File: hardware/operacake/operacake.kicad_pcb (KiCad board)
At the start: 4 copper layers, 120 x 75 mm, 152 parts, among them J1 CONN_02X20, J2 CONN_02X20, P1 ADDRESS, P20 GPIO, P22 I2S, P28 SD, P9 BASEBAND, U1 MASWSS0129, U10 74LVC1G58, U11 74LVC1G58, U12 74LVC1G58, U13 74LVC1G58, U14 74AHC1G02, U15 74AHC1G02, U16 74LVC1G19, U2 SKY13322, U3 SKY13322, U4 PCA9557, U5 TC7MBL3245CFT, U6 74LVC1G58, U7 74LVC1G58, U8 74AHC1G08, U9 74AHC1G08

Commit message: Moved via
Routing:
- net VCC: track 56.9 -> 55.6 mm
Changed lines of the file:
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@@
     (links 598)
     (no_connects 1)
-    (area 59.809499 99.809499 180.190501 175.190501)
+    (area 57.771558 99.809499 182.228443 175.190501)
     (thickness 1.6002)
     (drawings 148)
-    (tracks 1290)
+    (tracks 1287)
     (zones 0)
     (modules 152)
@@
   )
   (setup
-    (last_trace_width 0.2794)
+    (last_trace_width 0.3048)
     (user_trace_width 0.1524)
     (user_trace_width 0.2032)
@@
   (segment (start 131.50596 132.07238) (end 131.04622 132.53212) (width 0.2794) (layer C1F) (net 1))
   (segment (start 142.075 126.4919) (end 142.06728 126.49962) (width 0.2794) (layer C1F) (net 1))
+  (segment (start 132.55752 129.98196) (end 132.55752 129.06756) (width 0.3048) (layer C1F) (net 2) (status 400000))
+  (via (at 132.64896 128.97612) (size 1.0668) (drill 0.635) (layers C1F C4B) (net 2))
+  (segment (start 132.65 128.97508) (end 132.65 127.95) (width 0.3048) (layer C1F) (net 2) (status 800000))
+  (segment (start 128.80086 129.97434) (end 129.92862 129.97434) (width 0.2794) (layer C1F) (net 2) (status 400000))
+  (via (at 129.93116 129.9718) (size 1.0668) (drill 0.635) (layers C1F C4B) (net 2))
   (segment (start 127.87884 116.12118) (end 127.87884 116.49456) (width 0.2794) (layer C1F) (net 2))
   (via (at 128.31318 116.9289) (size 1.0668) (drill 0.635) (layers C1F C4B) (net 2))
@@
   (segment (start 116.336777 128.975619) (end 116.280396 129.032) (width 0.3048) (layer C1F) (net 2))
   (segment (start 116.280396 129.032) (end 114.9604 129.032) (width 0.3048) (layer C1F) (net 2))
-  (segment (start 132.65 127.95) (end 132.55752 128.04248) (width 0.3048) (layer C1F) (net 2) (status 30))
-  (segment (start 132.55752 128.04248) (end 132.55752 129.98196) (width 0.3048) (layer C1F) (net 2) (status 30))
-  (segment (start 132.55752 129.98196) (end 132.55752 129.7686) (width 0.3048) (layer C1F) (net 2) (status 30))
-  (segment (start 132.55752 129.7686) (end 133.28904 129.03708) (width 0.3048) (layer C1F) (net 2) (status 10))
-  (via (at 133.28904 129.03708) (size 1.0668) (drill 0.635) (layers C1F C4B) (net 2))
   (segment (start 128.65 127.95) (end 128.65 129.82348) (width 0.3048) (layer C1F) (net 2) (status 30))
-  (segment (start 128.65 129.82348) (end 128.95172 129.82348) (width 0.3048) (layer C1F) (net 2) (status 30))
-  (segment (start 128.95172 129.82348) (end 129.48666 129.28854) (width 0.3048) (layer C1F) (net 2) (status 10))
-  (via (at 129.48666 129.28854) (size 1.0668) (drill 0.635) (layers C1F C4B) (net 2))
   (segment (start 132.0546 120.61876) (end 132.0546 122.47626) (width 0.3048) (layer C1F) (net 2) (status 30))
   (segment (start 132.0546 122.47626) (end 131.93268 122.59818) (width 0.3048) (layer C1F) (net 2) (status 30))

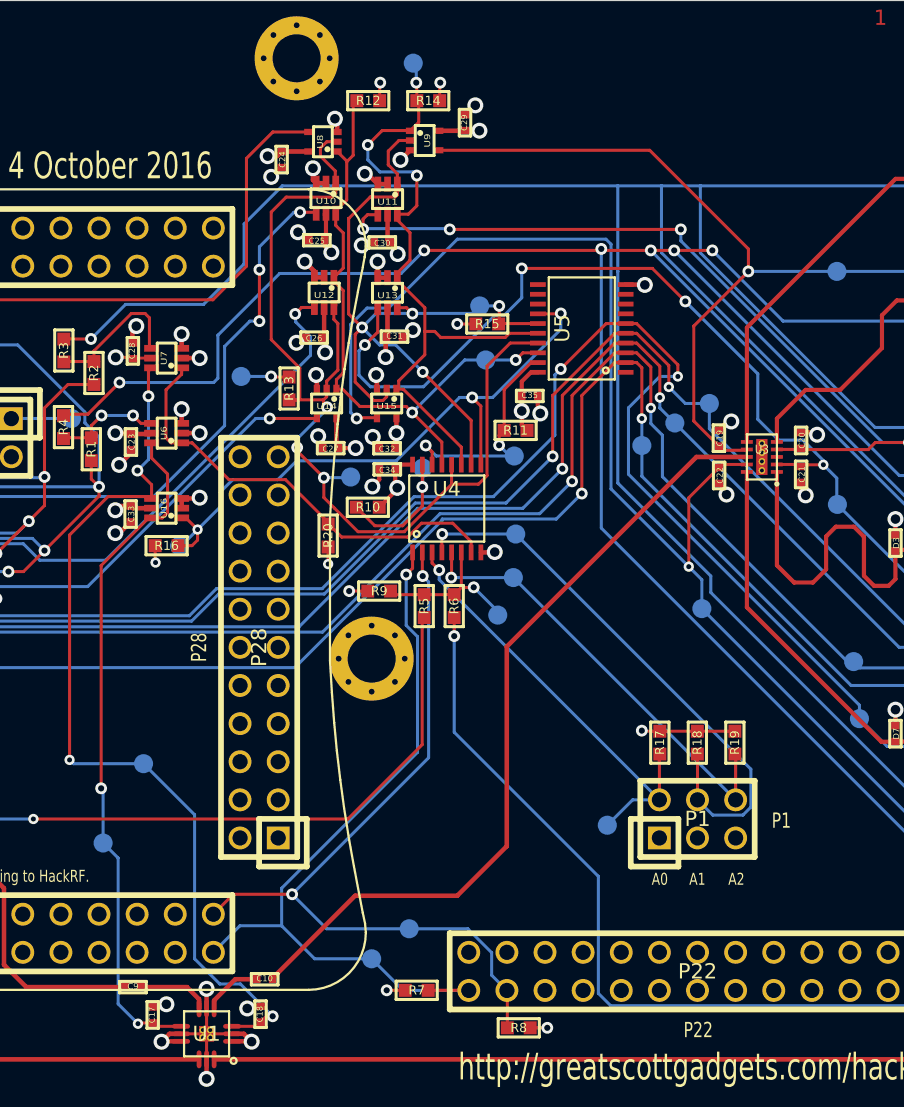
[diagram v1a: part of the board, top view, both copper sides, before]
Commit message: Moved vias.
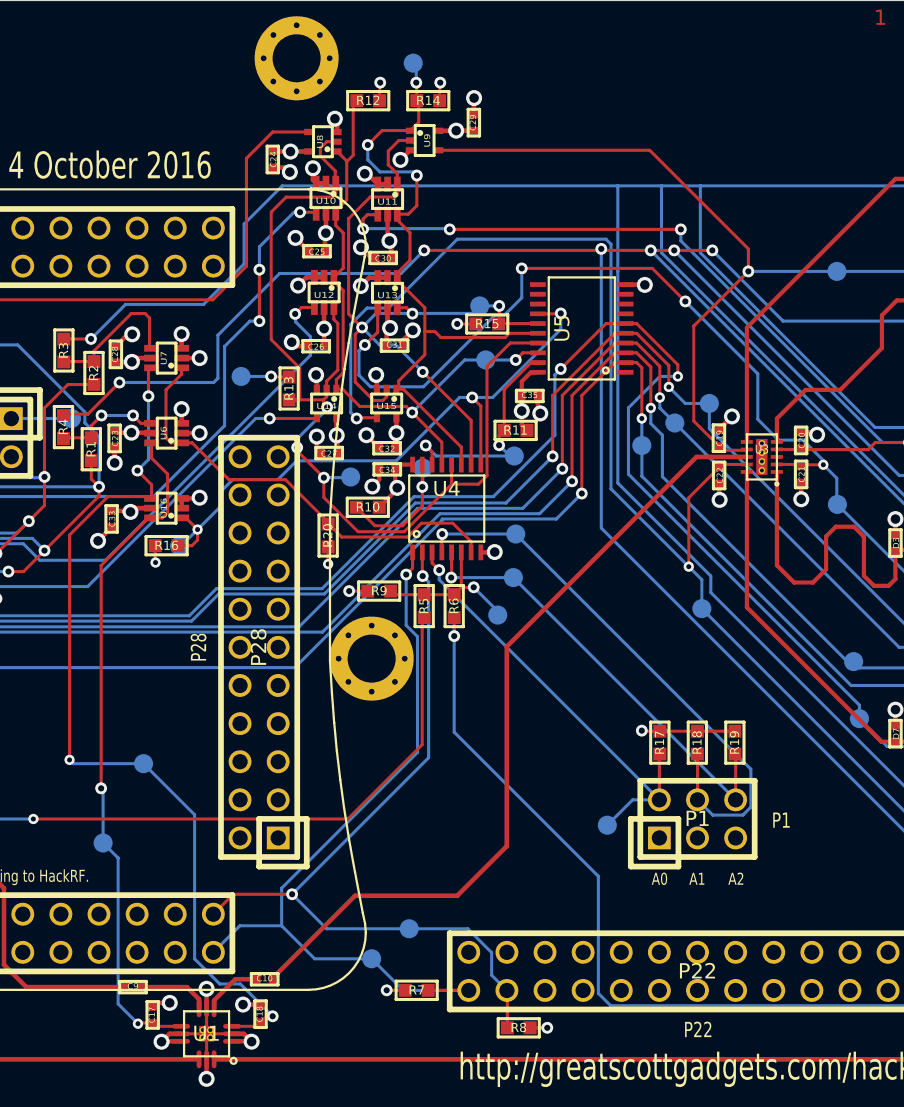
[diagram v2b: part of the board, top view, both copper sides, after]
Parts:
- moved C33 1.30 mm to (113.7, 134.7)
- moved C28 1.15 mm to (114.0, 123.7)
- moved C23 1.11 mm to (113.9, 129.3)
- moved C30 1.04 mm to (131.8, 117.3)
- moved C25 0.73 mm to (127.4, 116.9)
- moved C31 0.60 mm to (132.5, 123.1)
- moved C26 0.59 mm to (127.3, 123.2)
- moved C29 0.59 mm to (137.8, 108.3)
- moved C24 0.59 mm to (124.4, 110.7)
- moved C27 0.34 mm to (128.2, 130.3)
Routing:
- net VCC: track 55.6 -> 52.0 mm
- net GND: track 89.1 -> 92.6 mm

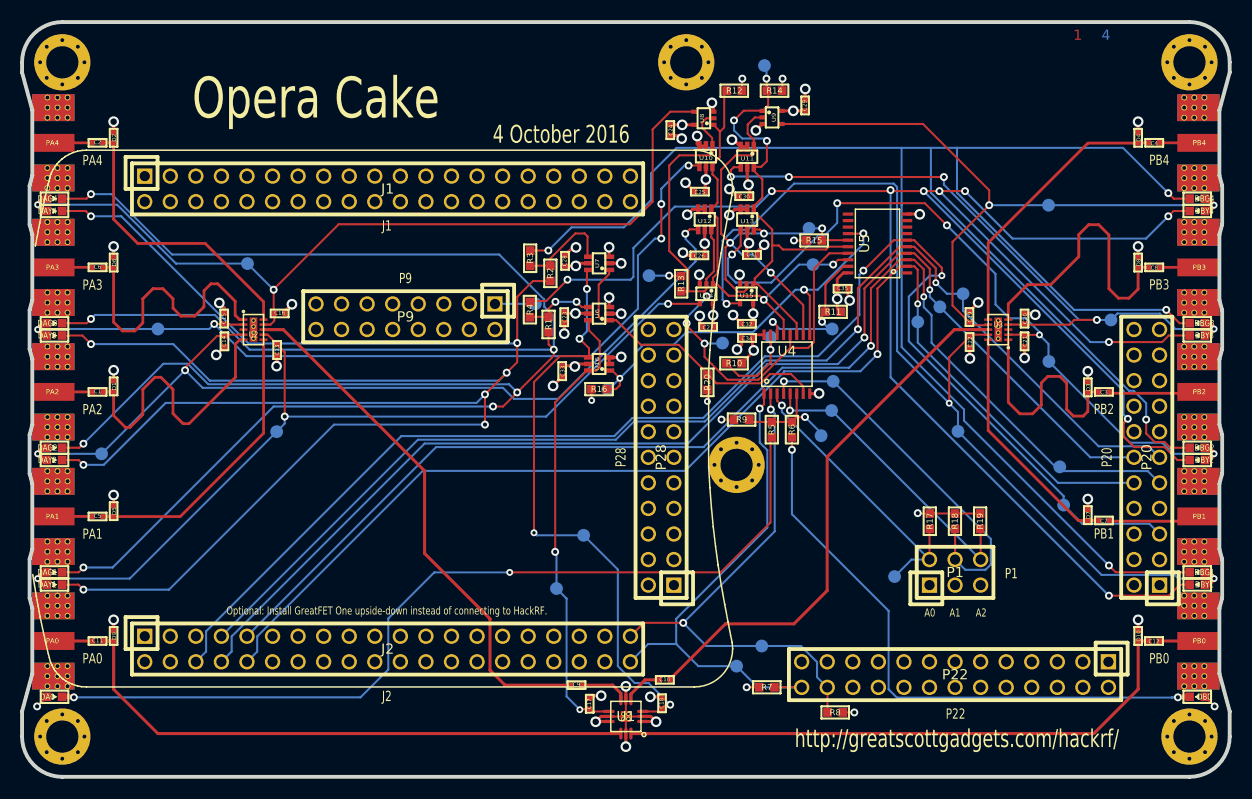
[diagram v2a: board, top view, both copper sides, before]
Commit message: Opera Cake: updated port names on silkscreen
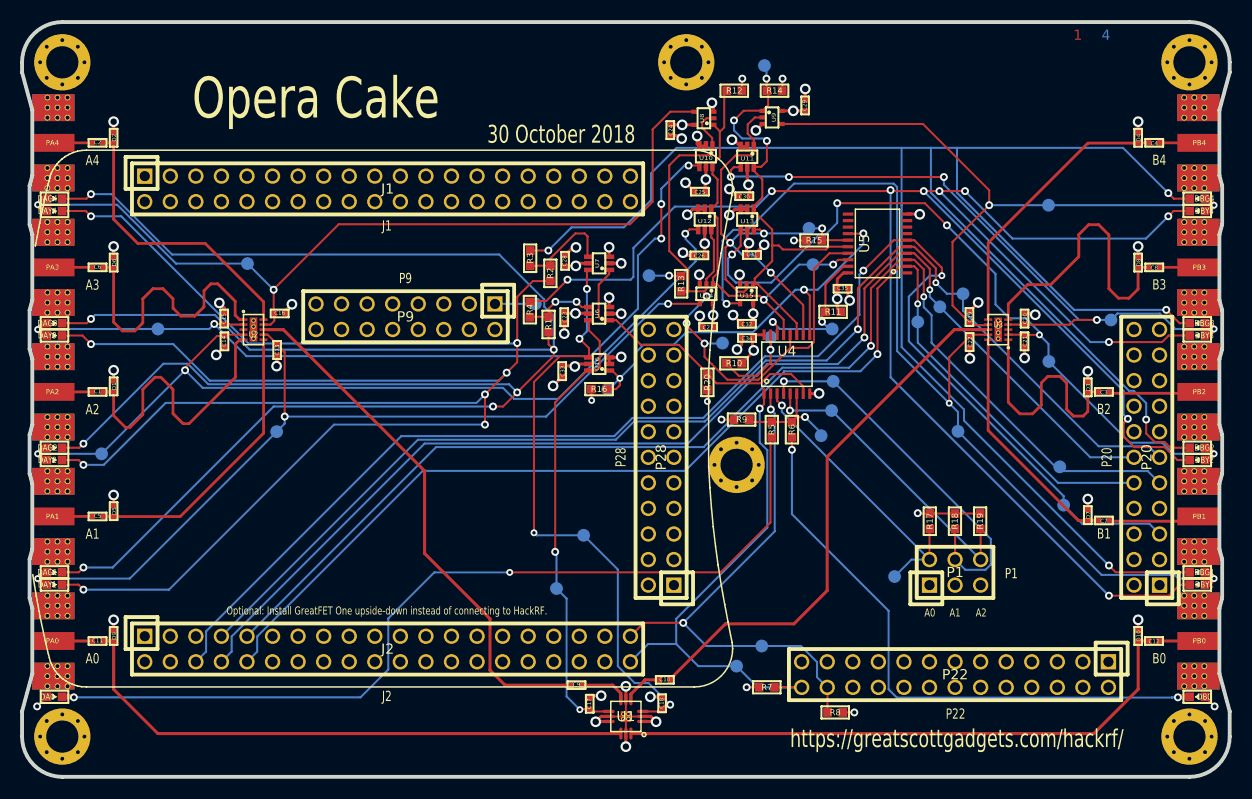
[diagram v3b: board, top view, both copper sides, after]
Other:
- board text added: "30 October 2018"
- board text added: "A3"
- board text added: "A4"
- board text added: "B0"
- board text added: "B1"
- board text added: "B2"
- board text added: "B3"
- board text added: "B4"
- board text added: "https://greatscottgadgets.com/hackrf/"
- board text removed: "4 October 2016"
- board text removed: "PA0"
- board text removed: "PA1"
- board text removed: "PA2"
- board text removed: "PA3"
- board text removed: "PA4"
- board text removed: "PB0"
- board text removed: "PB1"
- board text removed: "PB2"
- board text removed: "PB3"
- board text removed: "PB4"
- board text removed: "http://greatscottgadgets.com/hackrf/"
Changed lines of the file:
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@@
     (effects (font (size 0.8 0.6) (thickness 0.1)))
   )
-  (gr_text PB4 (at 173 113.725) (layer F.SilkS)
+  (gr_text B4 (at 173 113.725) (layer F.SilkS)
     (effects (font (size 1.016 0.762) (thickness 0.1905)))
   )
-  (gr_text PB3 (at 173 126.1) (layer F.SilkS)
+  (gr_text B3 (at 173 126.1) (layer F.SilkS)
     (effects (font (size 1.016 0.762) (thickness 0.1905)))
   )
-  (gr_text PB2 (at 167.5 138.475) (layer F.SilkS)
+  (gr_text B2 (at 167.5 138.475) (layer F.SilkS)
     (effects (font (size 1.016 0.762) (thickness 0.1905)))
   )
-  (gr_text PB1 (at 167.5 150.85) (layer F.SilkS)
+  (gr_text B1 (at 167.5 150.85) (layer F.SilkS)
     (effects (font (size 1.016 0.762) (thickness 0.1905)))
   )
-  (gr_text PB0 (at 173 163.25) (layer F.SilkS)
+  (gr_text B0 (at 173 163.25) (layer F.SilkS)
     (effects (font (size 1.016 0.762) (thickness 0.1905)))
   )
-  (gr_text PA4 (at 67 113.75) (layer F.SilkS)
+  (gr_text A4 (at 67 113.75) (layer F.SilkS)
     (effects (font (size 1.016 0.762) (thickness 0.1905)))
   )
-  (gr_text PA3 (at 67 126.125) (layer F.SilkS)
+  (gr_text A3 (at 67 126.125) (layer F.SilkS)
     (effects (font (size 1.016 0.762) (thickness 0.1905)))
   )
-  (gr_text PA2 (at 67 138.5) (layer F.SilkS)
+  (gr_text A2 (at 67 138.5) (layer F.SilkS)
     (effects (font (size 1.016 0.762) (thickness 0.1905)))
   )
-  (gr_text PA1 (at 67 150.875) (layer F.SilkS)
+  (gr_text A1 (at 67 150.875) (layer F.SilkS)
     (effects (font (size 1.016 0.762) (thickness 0.1905)))
   )
-  (gr_text PA0 (at 67 163.25) (layer F.SilkS)
+  (gr_text A0 (at 67 163.25) (layer F.SilkS)
     (effects (font (size 1.016 0.762) (thickness 0.1905)))
   )
@@
     (effects (font (size 1.016 1.016) (thickness 0.1778)))
   )
-  (gr_text "4 October 2016" (at 113.58 111.17) (layer F.SilkS)
+  (gr_text "30 October 2018" (at 113.58 111.17) (layer F.SilkS)
     (effects (font (size 1.778 1.27) (thickness 0.3048)))
   )
@@
     (effects (font (size 1.016 0.762) (thickness 0.1905)))
   )
-  (gr_text http://greatscottgadgets.com/hackrf/ (at 152.8878 171.2154) (layer F.SilkS)
+  (gr_text https://greatscottgadgets.com/hackrf/ (at 152.8878 171.2154) (layer F.SilkS)
     (effects (font (size 1.778 1.27) (thickness 0.3048)))
   )
